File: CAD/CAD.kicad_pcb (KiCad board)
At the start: 2 copper layers, 3 parts

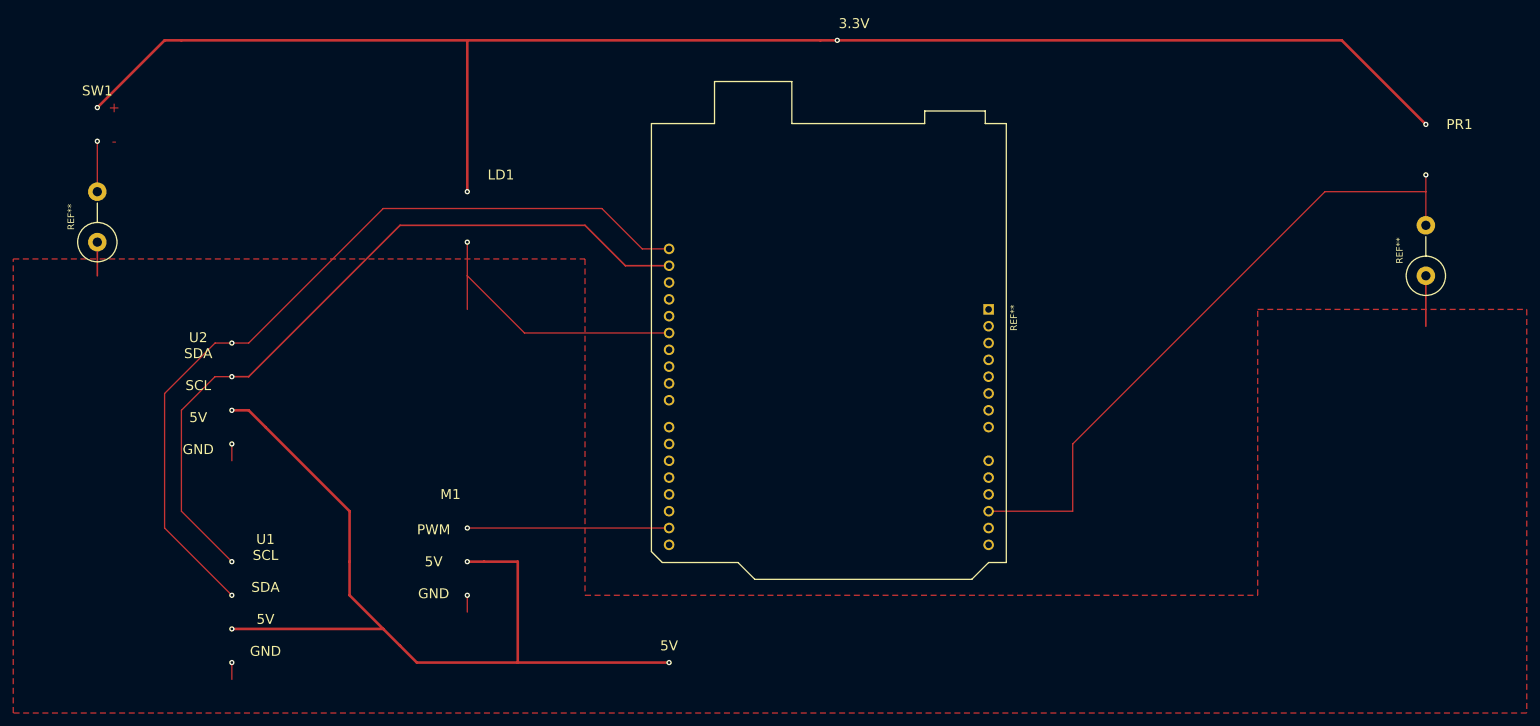
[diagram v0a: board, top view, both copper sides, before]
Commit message: updated pcb layout with template
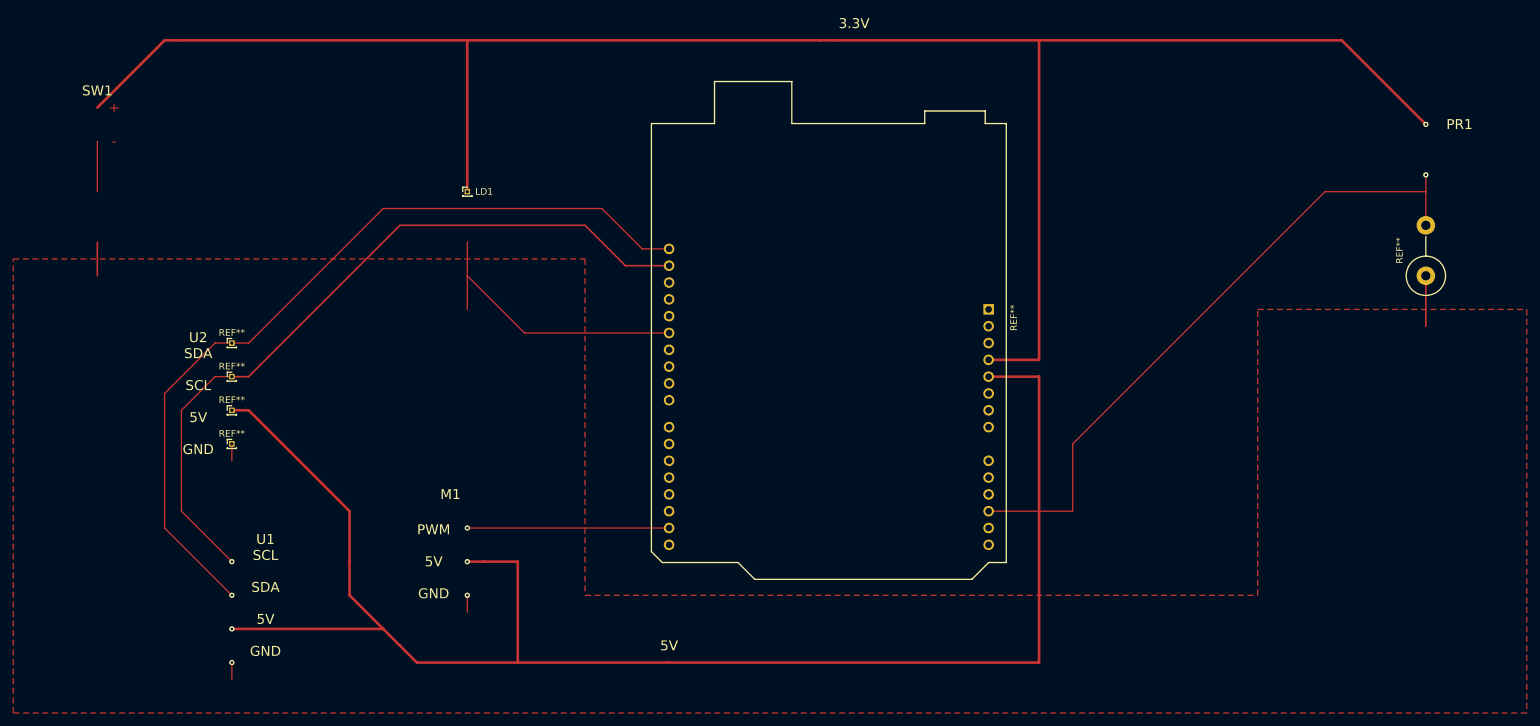
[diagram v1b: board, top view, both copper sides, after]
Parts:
- removed the REF** at (30.5, 61.0)
- added LD1: PinHeader_1x01_P1.00mm_Vertical, Connector_PinHeader_1.00mm:PinHeader_1x01_P1.00mm_Vertical, F.Cu at (86.4, 53.3)
- added REF**: PinHeader_1x01_P1.00mm_Vertical, Connector_PinHeader_1.00mm:PinHeader_1x01_P1.00mm_Vertical, F.Cu at (50.8, 81.3)
- added REF**: PinHeader_1x01_P1.00mm_Vertical, Connector_PinHeader_1.00mm:PinHeader_1x01_P1.00mm_Vertical, F.Cu at (50.8, 91.4)
- added REF**: PinHeader_1x01_P1.00mm_Vertical, Connector_PinHeader_1.00mm:PinHeader_1x01_P1.00mm_Vertical, F.Cu at (50.8, 86.4)
- added REF**: PinHeader_1x01_P1.00mm_Vertical, Connector_PinHeader_1.00mm:PinHeader_1x01_P1.00mm_Vertical, F.Cu at (50.8, 76.2)
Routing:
- net (no net): track 202.2 -> 730.2 mm, vias 19 -> 9
- net 33V: track 233.0 -> 0.00 mm
- net 5V: track 135.0 -> 0.00 mm
- net GND: track 0.00 -> 2.54 mm
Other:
- board text removed: "LD1"

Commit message: added BOM
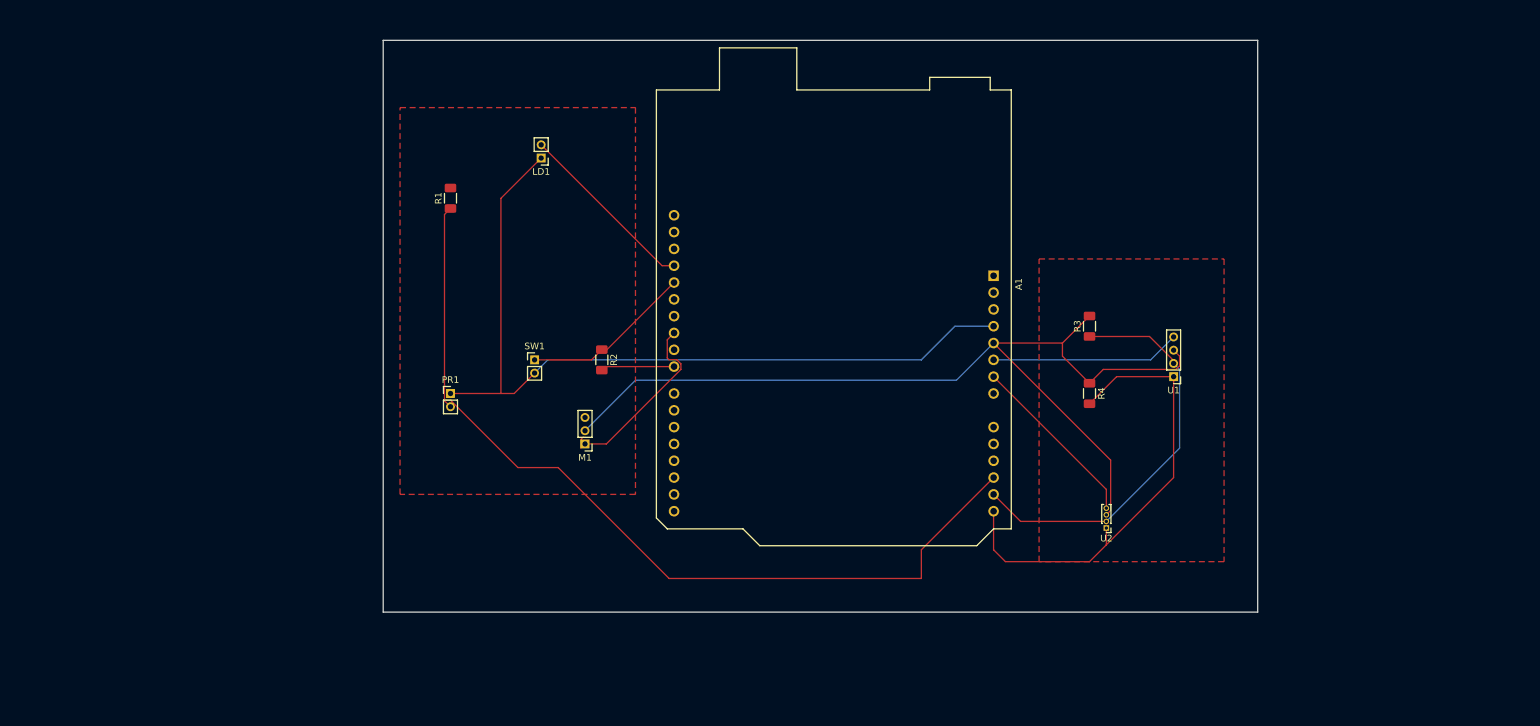
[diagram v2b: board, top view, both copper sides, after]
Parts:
- removed REF**: R_Axial_DIN0614_L14.3mm_D5.7mm_P7.62mm_Vertical, Resistor_THT:R_Axial_DIN0614_L14.3mm_D5.7mm_P7.62mm_Vertical
- removed REF** (x4): PinHeader_1x01_P1.00mm_Vertical, Connector_PinHeader_1.00mm:PinHeader_1x01_P1.00mm_Vertical
- removed REF**: Arduino_UNO_R3, Module:Arduino_UNO_R3
- added A1: Arduino_UNO_R3, Module:Arduino_UNO_R3, F.Cu at (165.8, 66.0)
- added M1: Motor_Servo_Hitec, Connector_PinHeader_2.00mm:PinHeader_1x03_P2.00mm_Vertical, F.Cu at (104.1, 91.4)
- added PR1: R_Photo, Connector_PinHeader_2.00mm:PinHeader_1x02_P2.00mm_Vertical, F.Cu at (83.8, 83.8)
- added R1: 100, Resistor_SMD:R_1206_3216Metric_Pad1.30x1.75mm_HandSolder, F.Cu at (83.8, 54.3)
- added R2: 10k, Resistor_SMD:R_1206_3216Metric_Pad1.30x1.75mm_HandSolder, F.Cu at (106.7, 78.7)
- added R3: 4.7k, Resistor_SMD:R_1206_3216Metric_Pad1.30x1.75mm_HandSolder, F.Cu at (180.3, 73.7)
- added R4: 4.7k, Resistor_SMD:R_1206_3216Metric_Pad1.30x1.75mm_HandSolder, F.Cu at (180.3, 83.8)
- added SW1: SW_Push, Connector_PinHeader_2.00mm:PinHeader_1x02_P2.00mm_Vertical, F.Cu at (96.5, 78.7)
- added U1: RFID_RC522, Connector_PinHeader_2.00mm:PinHeader_1x04_P2.00mm_Vertical, F.Cu at (193.0, 81.3)
- added U2: LCD_1602_I2C, Connector_PinHeader_1.00mm:PinHeader_1x04_P1.00mm_Vertical, F.Cu at (182.9, 104.1)
- LD1: value PinHeader_1x01_P1.00mm_Vertical -> D_Laser_1C2A; footprint Connector_PinHeader_1.00mm:PinHeader_1x01_P1.00mm_Vertical -> Connector_PinHeader_2.00mm:PinHeader_1x02_P2.00mm_Vertical
- moved LD1 12.3 mm to (97.5, 48.3), turned to 180 degrees
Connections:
- LD1 pad 1: (no net) -> +3.3V
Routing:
- net (no net): track 730.2 -> 0.00 mm, vias 9 -> 0
- net +5V: track 0.00 -> 142.1 mm
- net Net-(A1-Pad12): track 0.00 -> 133.4 mm
- net SDA: track 125.0 -> 0.00 mm
- net +3.3V: track 0.00 -> 124.3 mm
- net SCL: track 113.8 -> 0.00 mm
- net GND: track 2.54 -> 95.0 mm
- net Net-(A1-Pad14): track 0.00 -> 71.2 mm
- net Net-(A1-Pad13): track 0.00 -> 62.4 mm
- net Net-(A1-Pad25): track 0.00 -> 28.7 mm
- net Net-(A1-Pad28): track 0.00 -> 25.9 mm
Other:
- board outline added: 132.1 x 86.4 mm
- rule pad_to_mask_clearance: 0 -> 0.0508
- board text removed: "+"
- board text removed: "-"
- board text removed: "3.3V"
- board text removed: "5V"
- board text removed: "M1"
- board text removed: "PR1"
- board text removed: "PWM 5V GND"
- board text removed: "SW1"
- board text removed: "U1 SCL SDA 5V GND"
- board text removed: "U2 SDA SCL 5V GND"

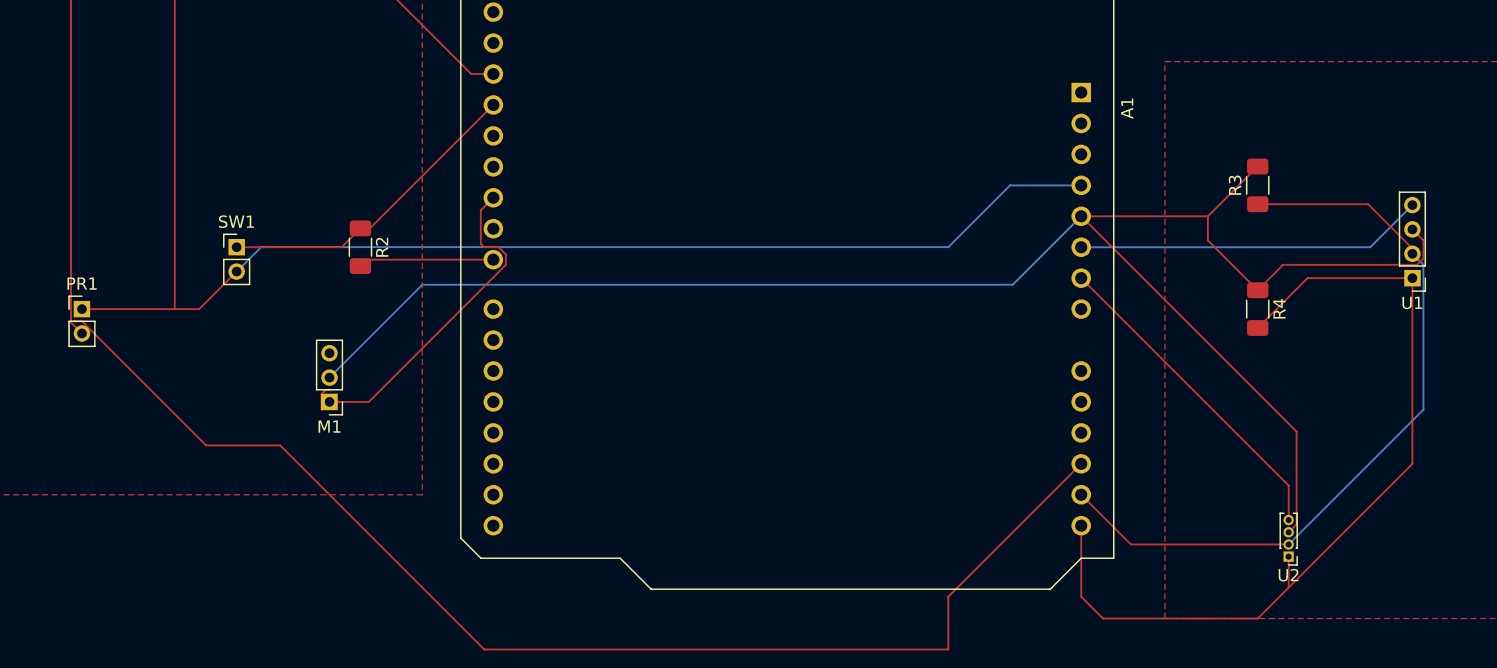
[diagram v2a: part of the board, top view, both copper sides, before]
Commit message: Fixed pcb footprints, passing DRC!
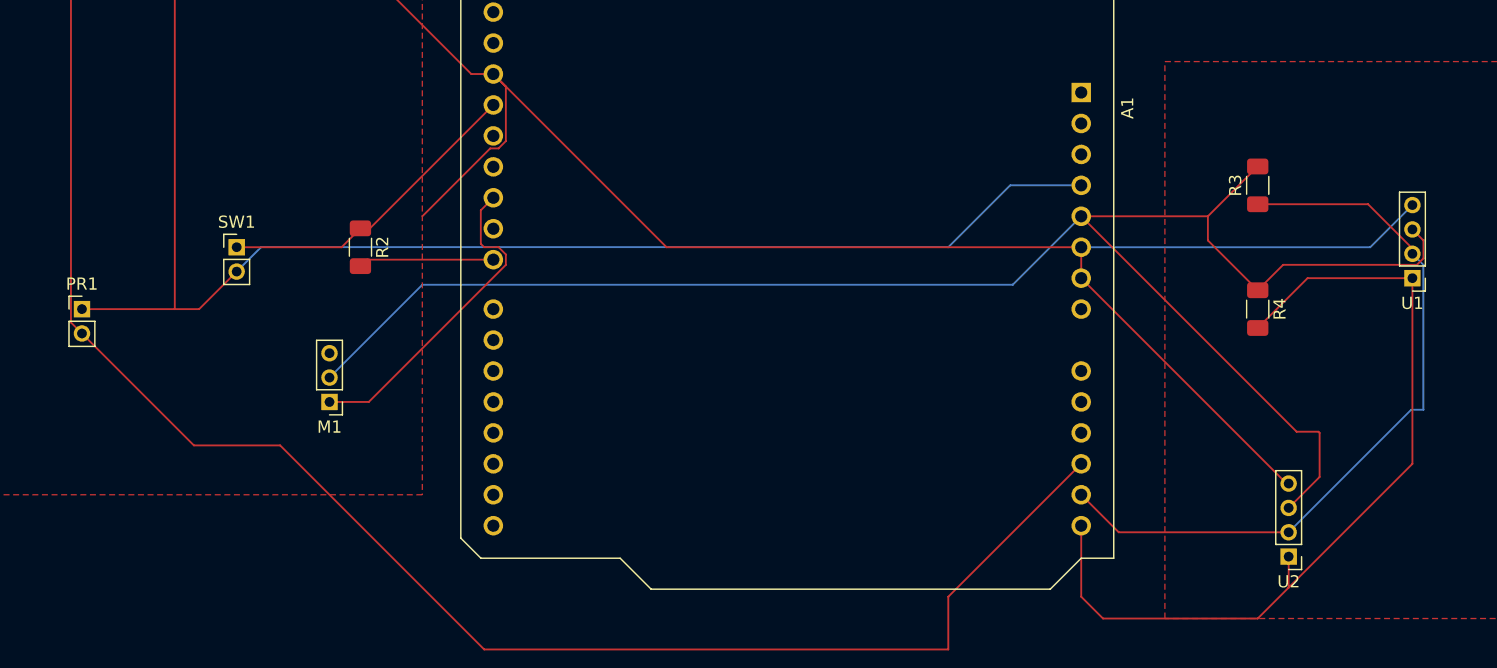
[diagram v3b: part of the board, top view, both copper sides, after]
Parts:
- U2: footprint Connector_PinHeader_1.00mm:PinHeader_1x04_P1.00mm_Vertical -> Connector_PinHeader_2.00mm:PinHeader_1x04_P2.00mm_Vertical
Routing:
- net GND: track 95.0 -> 163.5 mm
- net Net-(A1-Pad25): track 28.7 -> 26.6 mm
- net Net-(A1-Pad13): track 62.4 -> 61.2 mm
- net Net-(A1-Pad12): track 133.4 -> 132.3 mm
- net +5V: track 142.1 -> 142.7 mm

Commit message: Final CAD
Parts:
- added Q1: 2N7002, Package_TO_SOT_SMD:SOT-223-3_TabPin2, F.Cu at (118.1, 96.5)
- added R5: 10k, Resistor_SMD:R_1206_3216Metric_Pad1.30x1.75mm_HandSolder, F.Cu at (116.8, 114.3)
- added R6: 10k, Resistor_SMD:R_1206_3216Metric_Pad1.30x1.75mm_HandSolder, F.Cu at (116.8, 110.8)
- added R7: 10k, Resistor_SMD:R_1206_3216Metric_Pad1.30x1.75mm_HandSolder, F.Cu at (116.8, 107.3)
- added R8: 10k, Resistor_SMD:R_1206_3216Metric_Pad1.30x1.75mm_HandSolder, F.Cu at (116.8, 104.1)
- added SW2: SW_Push, Connector_PinHeader_2.54mm:PinHeader_1x02_P2.54mm_Vertical, F.Cu at (142.2, 99.1)
- A1: moved to B.Cu
- LD1: footprint Connector_PinHeader_2.00mm:PinHeader_1x02_P2.00mm_Vertical -> Connector_PinSocket_2.54mm:PinSocket_2x04_P2.54mm_Vertical
- M1: footprint Connector_PinHeader_2.00mm:PinHeader_1x03_P2.00mm_Vertical -> Connector_PinHeader_2.54mm:PinHeader_2x03_P2.54mm_Vertical
- PR1: footprint Connector_PinHeader_2.00mm:PinHeader_1x02_P2.00mm_Vertical -> Connector_PinHeader_2.54mm:PinHeader_2x04_P2.54mm_Vertical
- R1: value 100 -> 10k
- SW1: footprint Connector_PinHeader_2.00mm:PinHeader_1x02_P2.00mm_Vertical -> Connector_PinHeader_2.54mm:PinHeader_1x02_P2.54mm_Vertical
- U1: footprint Connector_PinHeader_2.00mm:PinHeader_1x04_P2.00mm_Vertical -> Connector_PinSocket_2.54mm:PinSocket_2x04_P2.54mm_Vertical
- U2: footprint Connector_PinHeader_2.00mm:PinHeader_1x04_P2.00mm_Vertical -> Connector_PinSocket_2.54mm:PinSocket_1x04_P2.54mm_Vertical
- moved R1 78.8 mm to (147.3, 101.0), turned to -90 degrees
- moved A1 60.5 mm to (106.7, 78.7)
- moved U2 56.7 mm to (139.7, 67.3), turned to 0 degrees
- moved PR1 55.2 mm to (131.4, 111.8), turned to 180 degrees
- moved U1 53.9 mm to (139.7, 88.9)
- moved SW1 48.2 mm to (142.2, 94.0), turned to -90 degrees
- moved LD1 47.8 mm to (132.1, 81.3), turned to 0 degrees
- moved R2 45.8 mm to (149.9, 94.0), turned to 90 degrees
- moved M1 37.5 mm to (137.2, 109.2), turned to 0 degrees
- moved R4 32.1 mm to (149.9, 73.7), turned to 90 degrees
- moved R3 31.1 mm to (149.9, 67.3)
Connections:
- A1 pad 10: unconnected-(A1-Pad10) -> Net-(A1-Pad10)
- A1 pad 11: unconnected-(A1-Pad11) -> Net-(A1-Pad11)
- A1 pad 13: Net-(A1-Pad13) -> unconnected-(A1-Pad13)
- A1 pad 14: Net-(A1-Pad14) -> unconnected-(A1-Pad14)
- A1 pad 17: unconnected-(A1-Pad17) -> Net-(A1-Pad17)
- A1 pad 18: unconnected-(A1-Pad18) -> Net-(A1-Pad18)
- A1 pad 19: unconnected-(A1-Pad19) -> Net-(A1-Pad19)
- A1 pad 20: unconnected-(A1-Pad20) -> Net-(A1-Pad20)
- A1 pad 21: unconnected-(A1-Pad21) -> Net-(A1-Pad21)
- A1 pad 22: unconnected-(A1-Pad22) -> Net-(A1-Pad22)
- A1 pad 23: GND -> Net-(A1-Pad23)
- A1 pad 24: unconnected-(A1-Pad24) -> Net-(A1-Pad24)
- A1 pad 26: unconnected-(A1-Pad26) -> Net-(A1-Pad26)
- A1 pad 27: unconnected-(A1-Pad27) -> Net-(A1-Pad27)
- A1 pad 31: unconnected-(A1-Pad31) -> Net-(A1-Pad31)
- A1 pad 32: unconnected-(A1-Pad32) -> Net-(A1-Pad32)
- A1 pad 9: unconnected-(A1-Pad9) -> Net-(A1-Pad9)
- LD1 pad 1: +3.3V -> Net-(LD1-Pad1)
- LD1 pad 2: GND -> +5V
- M1 pad 1: Net-(A1-Pad25) -> +9V
- M1 pad 2: +5V -> Net-(A1-Pad20)
- PR1 pad 1: +3.3V -> +5V
- R1 pad 1: Net-(A1-Pad12) -> Net-(A1-Pad21)
- R2 pad 1: Net-(A1-Pad28) -> Net-(A1-Pad22)
- R3 pad 1: Net-(A1-Pad13) -> Net-(A1-Pad32)
- R4 pad 2: Net-(A1-Pad14) -> Net-(A1-Pad31)
- SW1 pad 1: Net-(A1-Pad28) -> Net-(A1-Pad22)
- U1 pad 1: Net-(A1-Pad14) -> +3.3V
- U1 pad 2: Net-(A1-Pad13) -> Net-(A1-Pad24)
- U1 pad 3: +5V -> (no net)
- U1 pad 4: GND -> unconnected-(U1-Pad4)
- U2 pad 1: Net-(A1-Pad14) -> +5V
- U2 pad 2: Net-(A1-Pad13) -> Net-(A1-Pad32)
- U2 pad 3: +5V -> Net-(A1-Pad31)
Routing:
- net GND: track 163.5 -> 0.00 mm, vias 0 -> 19
- net Net-(A1-Pad12): track 132.3 -> 27.0 mm
- net Net-(A1-Pad14): track 71.2 -> 0.00 mm
- net +3.3V: track 124.3 -> 55.1 mm
- net Net-(A1-Pad13): track 61.2 -> 0.00 mm
- net +5V: track 142.7 -> 181.2 mm
- net Net-(A1-Pad23): track 0.00 -> 37.2 mm
- net Net-(LD1-Pad1): track 0.00 -> 34.8 mm
- net Net-(A1-Pad27): track 0.00 -> 27.7 mm
- net Net-(A1-Pad11): track 0.00 -> 25.9 mm
- net Net-(A1-Pad10): track 0.00 -> 25.6 mm
- net Net-(A1-Pad9): track 0.00 -> 24.3 mm
- net Net-(A1-Pad17): track 0.00 -> 20.8 mm
- net Net-(A1-Pad20): track 0.00 -> 18.4 mm
- net Net-(A1-Pad19): track 0.00 -> 18.4 mm
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- added copper zone on B.Cu, net GND
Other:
- board size 132.1 x 86.4 mm -> 55.9 x 57.8 mm
- rule pad_to_mask_clearance: 0.0508 -> 0.1016
- board text added: "+"
- board text added: "-"
- board text added: "2"
- board text added: "3 (PWM)"
- board text added: "3.3V"
- board text added: "4"
- board text added: "5"
- board text added: "5V SCL SDA GND"
- board text added: "GND"
- board text added: "IRQ"
- board text added: "MISO"
- board text added: "MOSI"
- board text added: "Portland State University Fall 2022 - ECE411 Practicum Group 10 v2.2 - 11/16/2022"
- board text added: "RST"
- board text added: "SCK"
- board text added: "SDA"
